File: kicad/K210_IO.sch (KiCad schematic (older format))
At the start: 9 parts, among them J1 Conn_01x24_MountingPin, U1 K210, U2 GD25LQ128D, U3 LSM6DS3

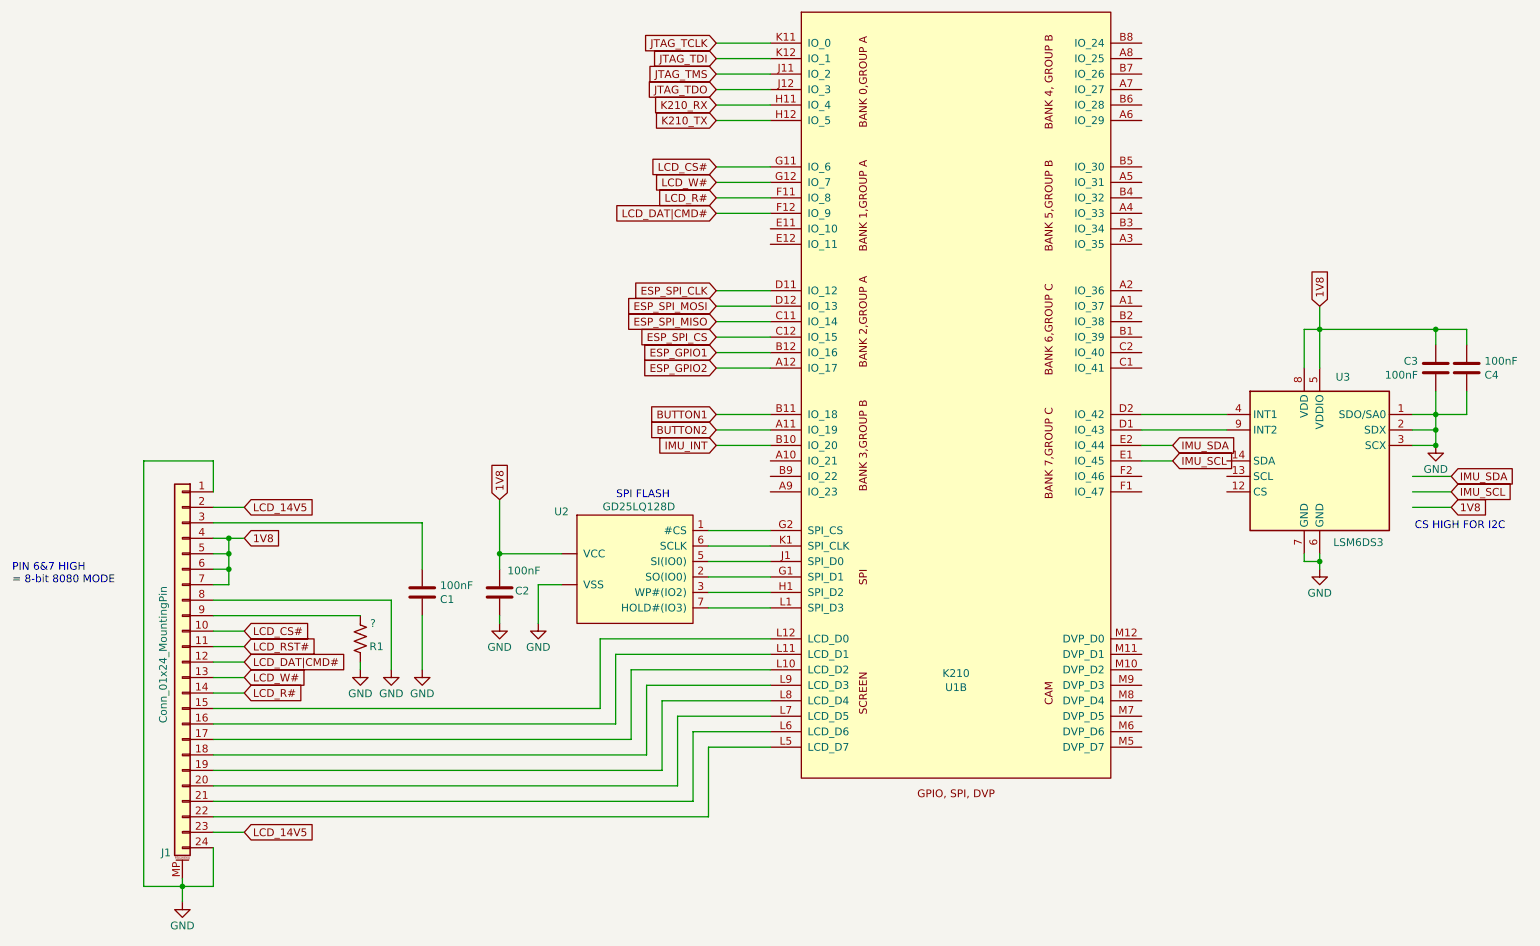
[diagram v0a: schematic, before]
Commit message: ESP32 added to schematic. ESP32 refs. Slight mod to block diagram.
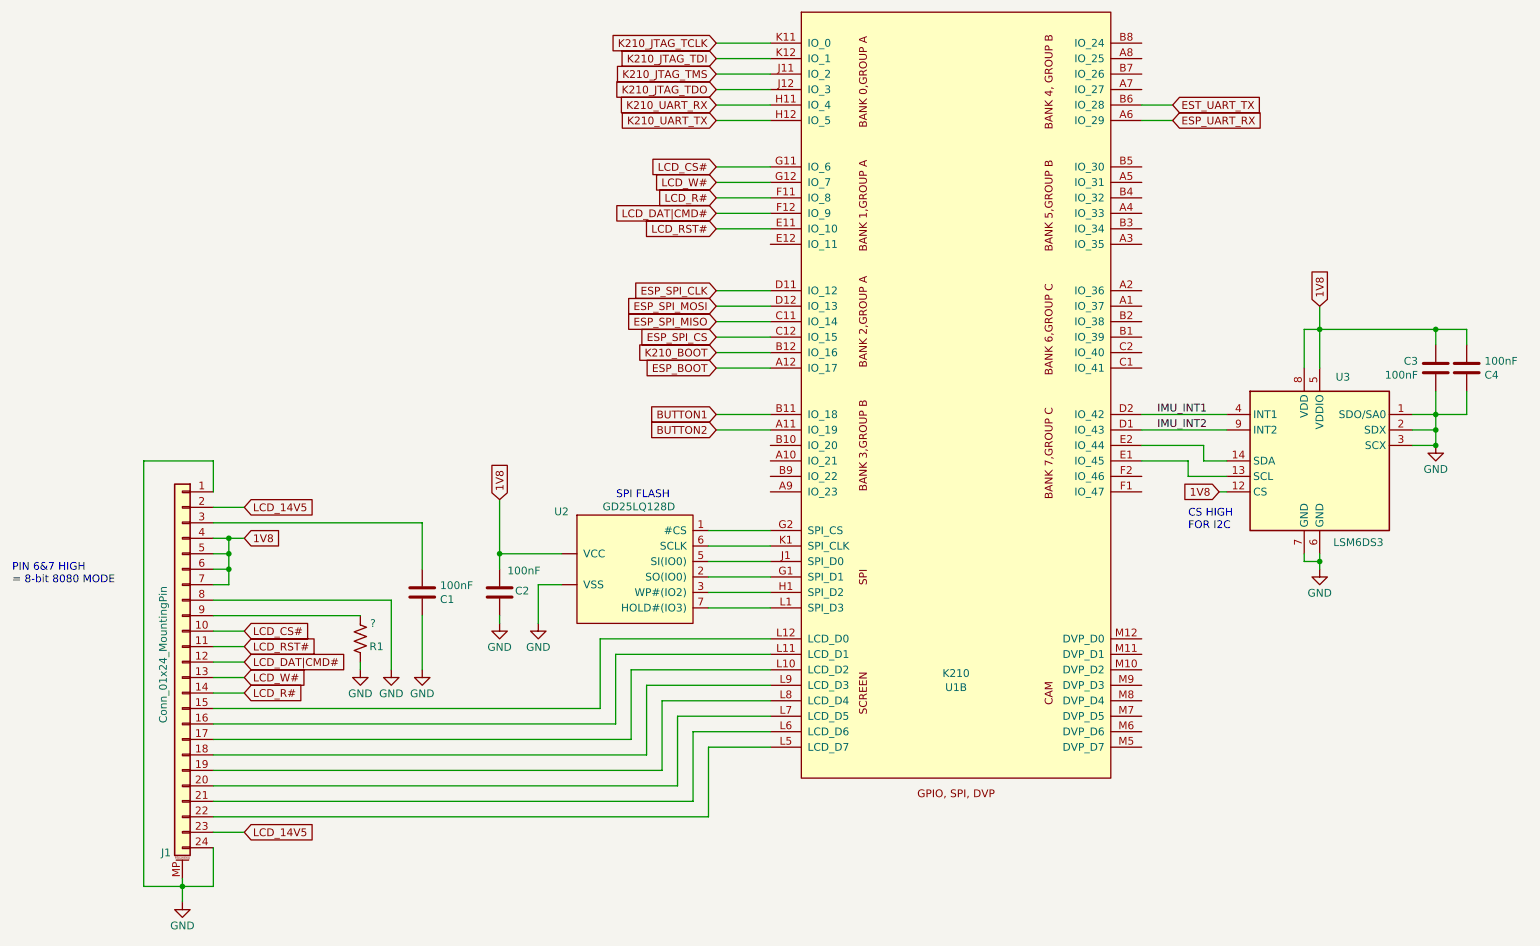
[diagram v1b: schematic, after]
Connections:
- net IMU_SCL is gone; now on an unnamed net: U1.E1 (IO_45)
- net IMU_SDA is gone; now on an unnamed net: U1.E2 (IO_44)
- net 1V8: now also U3.12 (CS)
- net LCD_RST#: now also U1.E11 (IO_10)
- net ESP_UART_RX: now reaches U1.A6 (IO_29)
- net EST_UART_TX: now reaches U1.B6 (IO_28)
- net IMU_INT2: now reaches U1.D1 (IO_43), U3.9 (INT2)
- net IMU_INT1: now reaches U1.D2 (IO_42), U3.4 (INT1)
- net ESP_GPIO1 renamed K210_BOOT
- net ESP_GPIO2 renamed ESP_BOOT
- net IMU_INT: no longer names the net of U1.B10 (IO_20)
- net JTAG_TCLK renamed K210_JTAG_TCLK
- net JTAG_TDI renamed K210_JTAG_TDI
- net JTAG_TDO renamed K210_JTAG_TDO
- net JTAG_TMS renamed K210_JTAG_TMS
- net K210_RX renamed K210_UART_RX
- net K210_TX renamed K210_UART_TX
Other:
- note added: "CS HIGH\nFOR I2C"
- note removed: "CS HIGH FOR I2C"
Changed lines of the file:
@@
 $Descr A4 11693 8268
 encoding utf-8
-Sheet 2 3
+Sheet 2 4
 Title ""
 Date ""
@@
 	5650 3750 6000 3750
 Wire Wire Line
-	5650 3850 6000 3850
-Wire Wire Line
 	6000 5800 5600 5800
 Wire Wire Line
@@
 	8400 3750 8950 3750
 Wire Wire Line
-	8400 3850 8600 3850
-Wire Wire Line
-	8400 3950 8600 3950
-Wire Wire Line
 	9450 3100 9450 3350
 Wire Wire Line
@@
 Wire Wire Line
 	10150 3850 10300 3850
-Wire Wire Line
-	10150 4050 10400 4050
-Wire Wire Line
-	10150 4150 10400 4150
-Wire Wire Line
-	10150 4250 10400 4250
 Wire Wire Line
 	10300 3100 10300 3200
@@
 Text Notes 5350 4200 2    50   ~ 0
 SPI FLASH
-Text Notes 10750 4400 2    50   ~ 0
-CS HIGH FOR I2C
+Text Notes 8700 4400 0    50   ~ 0
+CS HIGH\nFOR I2C
 Text GLabel 2600 4250 2    50   Input ~ 0
 LCD_14V5
@@
 1V8
 Text GLabel 5650 1250 0    50   Input ~ 0
-JTAG_TCLK
+K210_JTAG_TCLK
 Text GLabel 5650 1350 0    50   Input ~ 0
-JTAG_TDI
+K210_JTAG_TDI
 Text GLabel 5650 1450 0    50   Input ~ 0
-JTAG_TMS
+K210_JTAG_TMS
 Text GLabel 5650 1550 0    50   Input ~ 0
-JTAG_TDO
+K210_JTAG_TDO
 Text GLabel 5650 1650 0    50   Input ~ 0
-K210_RX
+K210_UART_RX
 Text GLabel 5650 1750 0    50   Input ~ 0
-K210_TX
+K210_UART_TX
 Text GLabel 5650 2050 0    50   Input ~ 0
 LCD_CS#
@@
 ESP_SPI_CS
 Text GLabel 5650 3250 0    50   Input ~ 0
-ESP_GPIO1
+K210_BOOT
 Text GLabel 5650 3350 0    50   Input ~ 0
-ESP_GPIO2
+ESP_BOOT
 Text GLabel 5650 3650 0    50   Input ~ 0
 BUTTON1
 Text GLabel 5650 3750 0    50   Input ~ 0
 BUTTON2
-Text GLabel 5650 3850 0    50   Input ~ 0
-IMU_INT
-Text GLabel 8600 3850 2    50   Input ~ 0
-IMU_SDA
-Text GLabel 8600 3950 2    50   Input ~ 0
-IMU_SCL
 Text GLabel 9550 2950 1    50   Input ~ 0
 1V8
-Text GLabel 10400 4050 2    50   Input ~ 0
-IMU_SDA
-Text GLabel 10400 4150 2    50   Input ~ 0
-IMU_SCL
-Text GLabel 10400 4250 2    50   Input ~ 0
+Text GLabel 8900 4150 0    50   Input ~ 0
 1V8
 $Comp
@@
 	1    0    0    -1
 $EndComp
+Text GLabel 5650 2450 0    50   Input ~ 0
+LCD_RST#
+Wire Wire Line
+	5650 2450 6000 2450
+Text GLabel 8600 1750 2    50   Input ~ 0
+ESP_UART_RX
+Text GLabel 8600 1650 2    50   Input ~ 0
+EST_UART_TX
+Wire Wire Line
+	8600 1650 8400 1650
+Wire Wire Line
+	8400 1750 8600 1750
+Wire Wire Line
+	8800 3850 8800 3950
+Wire Wire Line
+	8800 3950 8950 3950
+Wire Wire Line
+	8400 3850 8800 3850
+Wire Wire Line
+	8950 4050 8700 4050
+Wire Wire Line
+	8700 4050 8700 3950
+Wire Wire Line
+	8400 3950 8700 3950
+Wire Wire Line
+	8900 4150 8950 4150
+Text Label 8500 3750 0    50   ~ 0
+IMU_INT2
+Text Label 8500 3650 0    50   ~ 0
+IMU_INT1
 $EndSCHEMATC

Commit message: 3 output SMPS added MIC23450
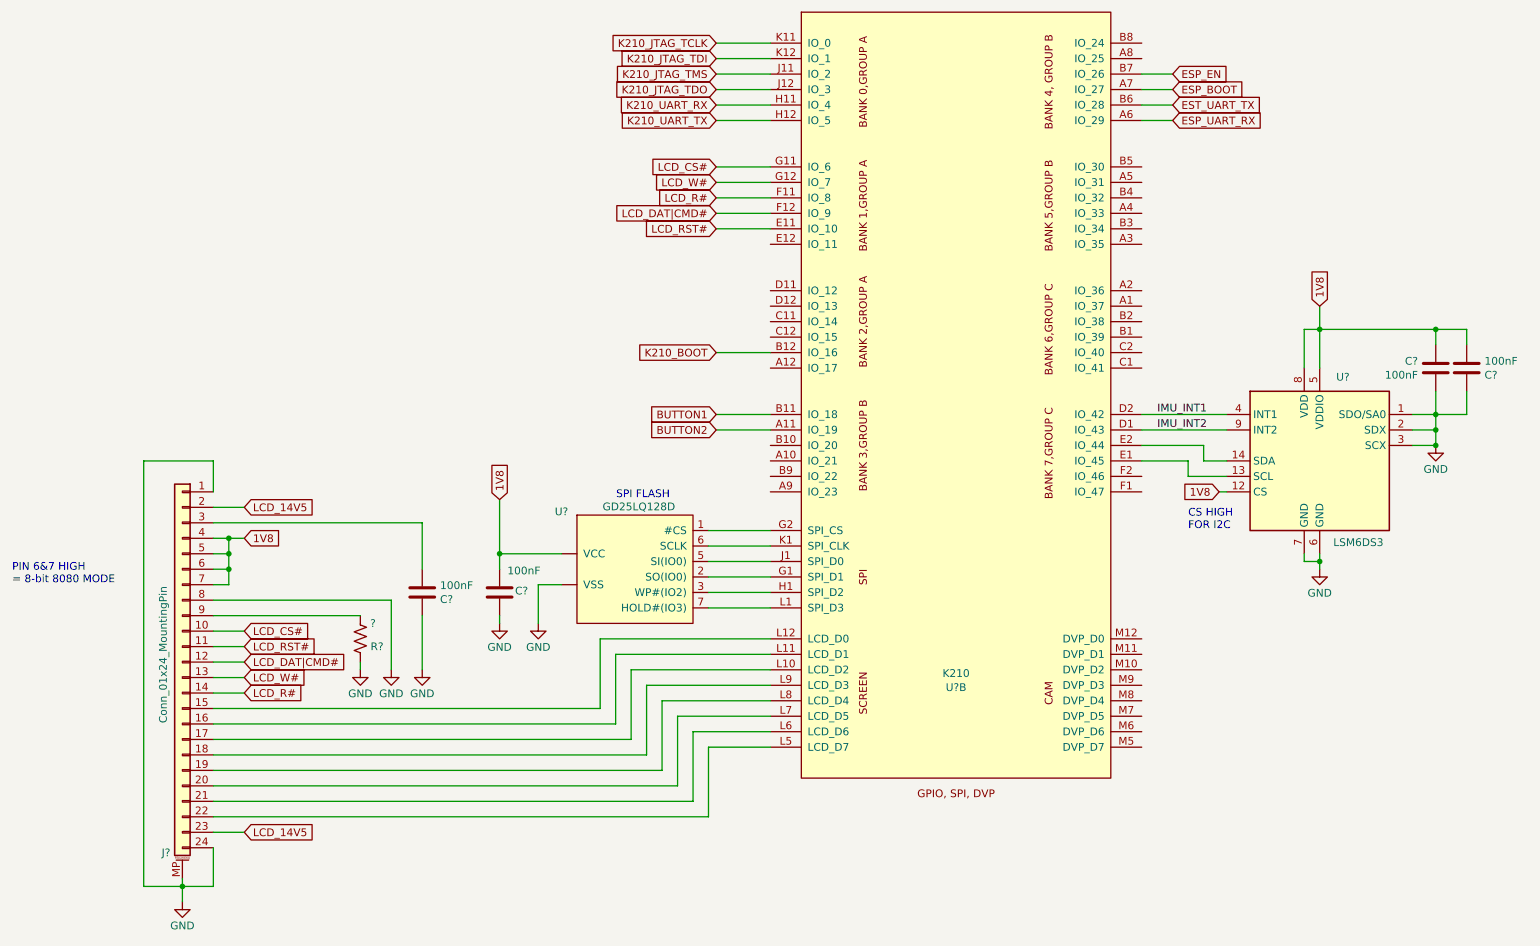
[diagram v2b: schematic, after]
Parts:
- renumbered C2 to C?, C3 to C?, C4 to C?, C1 to C?, J1 to J?, R1 to R?, U1 to U?, U2 to U?, U3 to U?
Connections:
- net ESP_BOOT: now also U?.A7 (IO_27); no longer U?.A12 (IO_17)
- net ESP_EN: now reaches U?.B7 (IO_26)
- net ESP_SPI_CLK: no longer names the net of U?.D11 (IO_12)
- net ESP_SPI_CS: no longer names the net of U?.C12 (IO_15)
- net ESP_SPI_MISO: no longer names the net of U?.C11 (IO_14)
- net ESP_SPI_MOSI: no longer names the net of U?.D12 (IO_13)
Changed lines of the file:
@@
 $Descr A4 11693 8268
 encoding utf-8
-Sheet 2 4
+Sheet 2 5
 Title ""
 Date ""
@@
 	5650 2350 6000 2350
 Wire Wire Line
-	5650 2850 6000 2850
-Wire Wire Line
-	5650 2950 6000 2950
-Wire Wire Line
-	5650 3050 6000 3050
-Wire Wire Line
-	5650 3150 6000 3150
-Wire Wire Line
 	5650 3250 6000 3250
-Wire Wire Line
-	5650 3350 6000 3350
 Wire Wire Line
 	5650 3650 6000 3650
@@
 Text GLabel 5650 2350 0    50   Input ~ 0
 LCD_DAT|CMD#
-Text GLabel 5650 2850 0    50   Input ~ 0
-ESP_SPI_CLK
-Text GLabel 5650 2950 0    50   Input ~ 0
-ESP_SPI_MOSI
-Text GLabel 5650 3050 0    50   Input ~ 0
-ESP_SPI_MISO
-Text GLabel 5650 3150 0    50   Input ~ 0
-ESP_SPI_CS
 Text GLabel 5650 3250 0    50   Input ~ 0
 K210_BOOT
-Text GLabel 5650 3350 0    50   Input ~ 0
+Text GLabel 8600 1550 2    50   Input ~ 0
 ESP_BOOT
 Text GLabel 5650 3650 0    50   Input ~ 0
@@
 1V8
 $Comp
-L power:GND #PWR0101
+L power:GND #PWR?
 U 1 1 5EB351B6
 P 2200 6800
-F 0 "#PWR0101" H 2200 6550 50  0001 C CNN
+F 0 "#PWR?" H 2200 6550 50  0001 C CNN
 F 1 "GND" H 2200 6646 50  0000 C CNN
 F 2 "" H 2200 6800 50  0001 C CNN
@@
 $EndComp
 $Comp
-L power:GND #PWR0102
+L power:GND #PWR?
 U 1 1 5EB8737E
 P 3350 5300
-F 0 "#PWR0102" H 3350 5050 50  0001 C CNN
+F 0 "#PWR?" H 3350 5050 50  0001 C CNN
 F 1 "GND" H 3350 5146 50  0000 C CNN
 F 2 "" H 3350 5300 50  0001 C CNN
@@
 $EndComp
 $Comp
-L power:GND #PWR0103
+L power:GND #PWR?
 U 1 1 5EB819C7
 P 3550 5300
-F 0 "#PWR0103" H 3550 5050 50  0001 C CNN
+F 0 "#PWR?" H 3550 5050 50  0001 C CNN
 F 1 "GND" H 3550 5146 50  0000 C CNN
 F 2 "" H 3550 5300 50  0001 C CNN
@@
 $EndComp
 $Comp
-L power:GND #PWR0104
+L power:GND #PWR?
 U 1 1 5EB5630E
 P 3750 5300
-F 0 "#PWR0104" H 3750 5050 50  0001 C CNN
+F 0 "#PWR?" H 3750 5050 50  0001 C CNN
 F 1 "GND" H 3750 5146 50  0000 C CNN
 F 2 "" H 3750 5300 50  0001 C CNN
@@
 $EndComp
 $Comp
-L power:GND #PWR0105
+L power:GND #PWR?
 U 1 1 5E982078
 P 4250 5000
-F 0 "#PWR0105" H 4250 4750 50  0001 C CNN
+F 0 "#PWR?" H 4250 4750 50  0001 C CNN
 F 1 "GND" H 4250 4846 50  0000 C CNN
 F 2 "" H 4250 5000 50  0001 C CNN
@@
 $EndComp
 $Comp
-L power:GND #PWR0106
+L power:GND #PWR?
 U 1 1 5E975272
 P 4500 5000
-F 0 "#PWR0106" H 4500 4750 50  0001 C CNN
+F 0 "#PWR?" H 4500 4750 50  0001 C CNN
 F 1 "GND" H 4500 4846 50  0000 C CNN
 F 2 "" H 4500 5000 50  0001 C CNN
@@
 $EndComp
 $Comp
-L power:GND #PWR0107
+L power:GND #PWR?
 U 1 1 5EAB3945
 P 9550 4650
-F 0 "#PWR0107" H 9550 4400 50  0001 C CNN
+F 0 "#PWR?" H 9550 4400 50  0001 C CNN
 F 1 "GND" H 9550 4496 50  0000 C CNN
 F 2 "" H 9550 4650 50  0001 C CNN
@@
 $EndComp
 $Comp
-L power:GND #PWR0108
+L power:GND #PWR?
 U 1 1 5EAC1BBD
 P 10300 3850
-F 0 "#PWR0108" H 10300 3600 50  0001 C CNN
+F 0 "#PWR?" H 10300 3600 50  0001 C CNN
 F 1 "GND" H 10300 3696 50  0000 C CNN
 F 2 "" H 10300 3850 50  0001 C CNN
@@
 $EndComp
 $Comp
-L Device:R_US R1
+L Device:R_US R?
 U 1 1 5EB82B2E
 P 3350 5100
-F 0 "R1" H 3500 5050 50  0000 R CNN
+F 0 "R?" H 3500 5050 50  0000 R CNN
 F 1 "?" H 3450 5200 50  0000 R CNN
 F 2 "" V 3390 5090 50  0001 C CNN
@@
 $EndComp
 $Comp
-L Device:C C1
+L Device:C C?
 U 1 1 5EB52F95
 P 3750 4800
-F 0 "C1" H 3865 4755 50  0000 L CNN
+F 0 "C?" H 3865 4755 50  0000 L CNN
 F 1 "100nF" H 3865 4845 50  0000 L CNN
 F 2 "" H 3788 4650 50  0001 C CNN
@@
 $EndComp
 $Comp
-L Device:C C2
+L Device:C C?
 U 1 1 5E97DA2D
 P 4250 4800
-F 0 "C2" H 4350 4810 50  0000 L CNN
+F 0 "C?" H 4350 4810 50  0000 L CNN
 F 1 "100nF" H 4300 4940 50  0000 L CNN
 F 2 "" H 4288 4650 50  0001 C CNN
@@
 $EndComp
 $Comp
-L Device:C C3
+L Device:C C?
 U 1 1 5EACAFF2
 P 10300 3350
-F 0 "C3" H 10415 3305 50  0000 L CNN
+F 0 "C?" H 10415 3305 50  0000 L CNN
 F 1 "100nF" H 10415 3395 50  0000 L CNN
 F 2 "" H 10338 3200 50  0001 C CNN
@@
 $EndComp
 $Comp
-L Device:C C4
+L Device:C C?
 U 1 1 5EACCA9A
 P 10500 3350
-F 0 "C4" H 10615 3305 50  0000 L CNN
+F 0 "C?" H 10615 3305 50  0000 L CNN
 F 1 "100nF" H 10615 3395 50  0000 L CNN
 F 2 "" H 10538 3200 50  0001 C CNN
@@
 $EndComp
 $Comp
-L Memory_Flash:GD25LQ128D U2
+L Memory_Flash:GD25LQ128D U?
 U 1 1 5E970C62
 P 5150 4650
-F 0 "U2" H 4650 5022 50  0000 C CNN
+F 0 "U?" H 4650 5022 50  0000 C CNN
 F 1 "GD25LQ128D" H 5150 5054 50  0000 C CNN
 F 2 "" H 5200 4750 50  0001 C CNN
@@
 $EndComp
 $Comp
-L Connector_Generic_MountingPin:Conn_01x24_MountingPin J1
+L Connector_Generic_MountingPin:Conn_01x24_MountingPin J?
 U 1 1 5EAE62DE
 P 2200 5250
-F 0 "J1" H 2306 4018 50  0000 C CNN
+F 0 "J?" H 2306 4018 50  0000 C CNN
 F 1 "Conn_01x24_MountingPin" V 2324 5298 50  0000 C CNN
 F 2 "" H 2200 5250 50  0001 C CNN
@@
 $EndComp
 $Comp
-L Sensor_Motion:LSM6DS3 U3
+L Sensor_Motion:LSM6DS3 U?
 U 1 1 5EA9FC8D
 P 9550 3950
-F 0 "U3" H 9400 4492 50  0000 C CNN
+F 0 "U?" H 9400 4492 50  0000 C CNN
 F 1 "LSM6DS3" H 9300 3423 50  0000 C CNN
 F 2 "Package_LGA:LGA-14_3x2.5mm_P0.5mm_LayoutBorder3x4y" H 9150 3250 50  0001 L CNN
@@
 $EndComp
 $Comp
-L Kendryte:K210 U1
+L Kendryte:K210 U?
 U 2 1 5E8F30E2
 P 7200 3150
-F 0 "U1" H 7200 886 50  0000 C CNN
+F 0 "U?" H 7200 886 50  0000 C CNN
 F 1 "K210" H 7200 977 50  0000 C CNN
 F 2 "" H 7900 5050 50  0001 C CNN
@@
 Text Label 8500 3650 0    50   ~ 0
 IMU_INT1
+Wire Wire Line
+	8600 1550 8400 1550
+Wire Wire Line
+	8400 1450 8600 1450
+Text GLabel 8600 1450 2    50   Input ~ 0
+ESP_EN
 $EndSCHEMATC
